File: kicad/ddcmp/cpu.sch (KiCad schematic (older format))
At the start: 9 parts, among them J1 UART, J4 LOOPTEST, U1 Pico

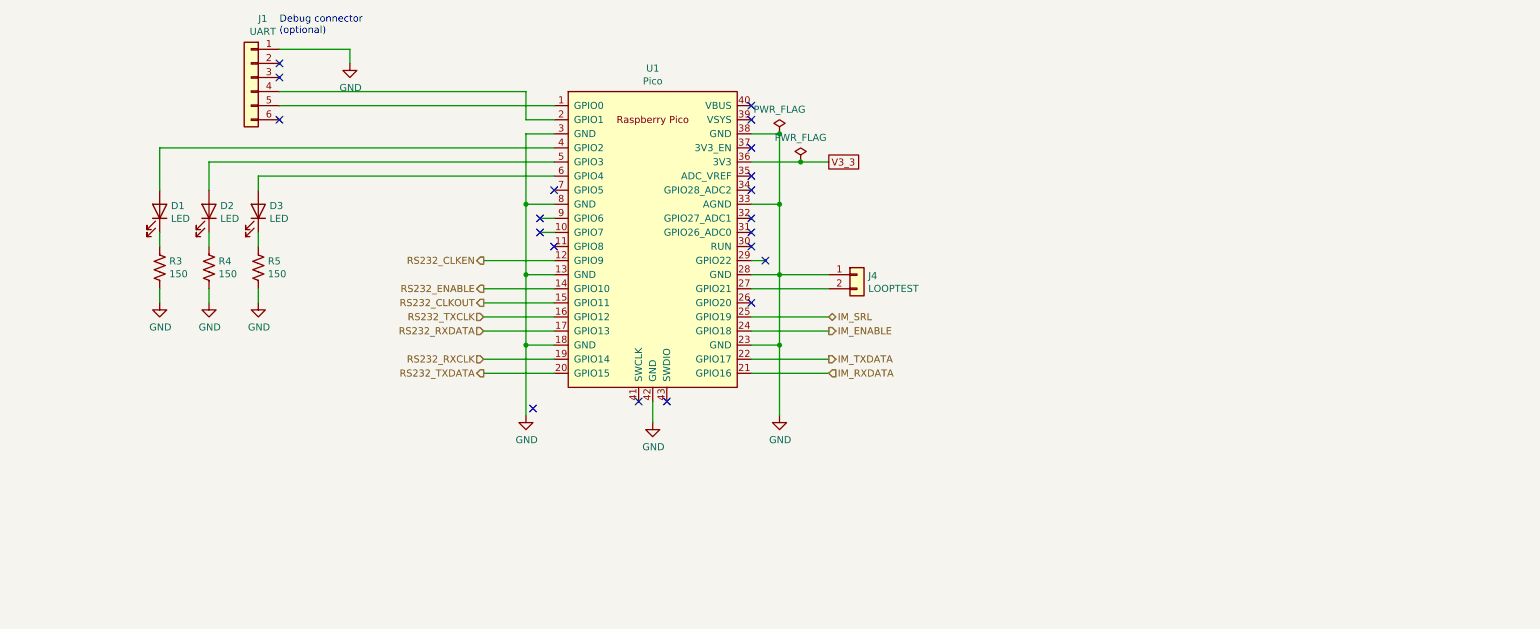
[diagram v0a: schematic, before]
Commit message: Finish the connector hookups, to be verified carefully against DMR-11 schematics.
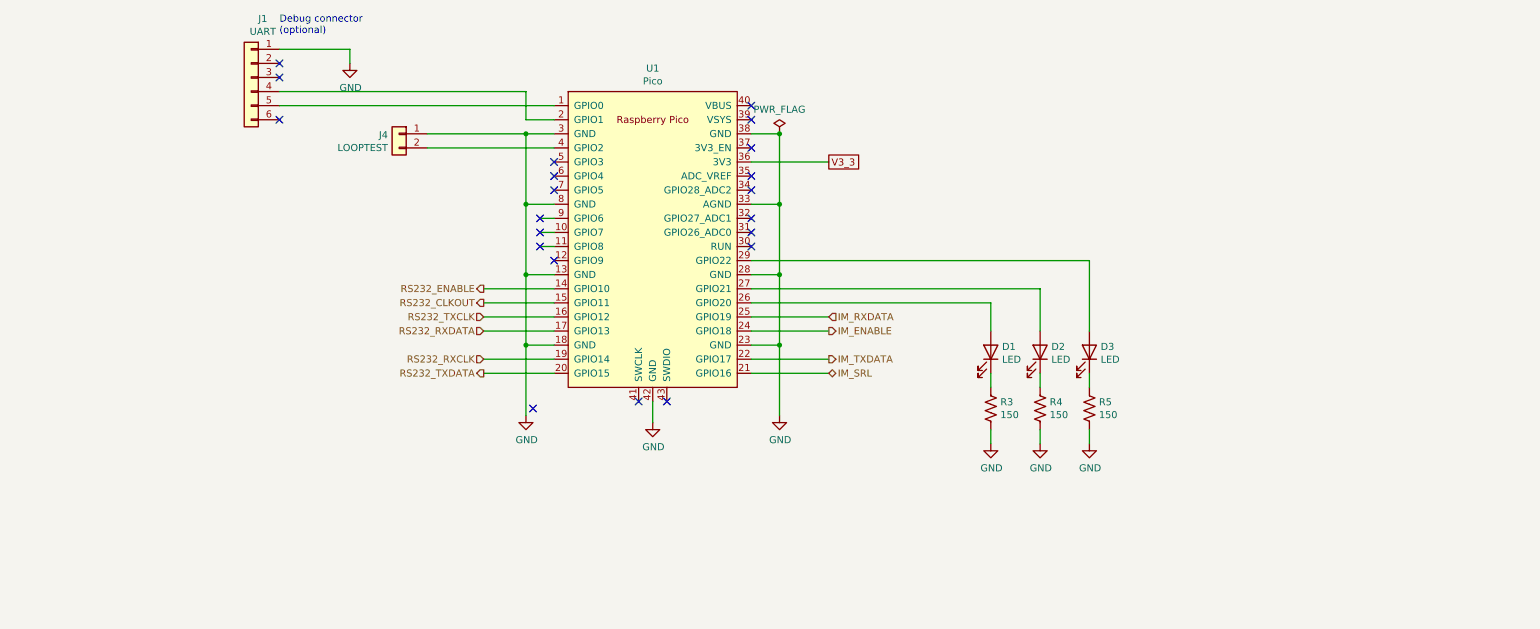
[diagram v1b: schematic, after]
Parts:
- U1: footprint RPi_Pico:RPi_Pico_SMD_TH -> ddcmp_parts:RPi_Pico_SMD_TH
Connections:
- net IM_RXDATA: now also U1.25 (GPIO19); no longer U1.21 (GPIO16)
- net IM_SRL: now also U1.21 (GPIO16); no longer U1.25 (GPIO19)
- net at U1.26 (GPIO20): now also D1.2 (A)
- net at U1.27 (GPIO21): now also D2.2 (A); no longer J4.2 (Pin_2)
- net at U1.29 (GPIO22): now also D3.2 (A)
- net at U1.4 (GPIO2): now also J4.2 (Pin_2); no longer D1.2 (A)
- net at U1.5 (GPIO3): no longer D2.2 (A)
- net at U1.6 (GPIO4): no longer D3.2 (A)
- net RS232_CLKEN: no longer names the net of U1.12 (GPIO9)
- no-connect marks 20 -> 21
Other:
- moved on the sheet: D1, D2, D3, J4, R3, R4, R5
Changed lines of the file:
@@
 Wire Wire Line
 	5050 4250 5050 4750
-Wire Wire Line
-	6650 2950 7000 2950
 Text GLabel 7200 2950 2    50   UnSpc ~ 0
 V3_3
@@
 L Device:LED D1
 U 1 1 60AC703D
-P 2450 3300
-F 0 "D1" V 2489 3380 50  0000 L CNN
-F 1 "LED" V 2398 3380 50  0000 L CNN
-F 2 "LEDs:LED_D3.0mm" H 2450 3300 50  0001 C CNN
-F 3 "~" H 2450 3300 50  0001 C CNN
-	1    2450 3300
+P 8350 4300
+F 0 "D1" V 8389 4380 50  0000 L CNN
+F 1 "LED" V 8298 4380 50  0000 L CNN
+F 2 "LEDs:LED_D3.0mm" H 8350 4300 50  0001 C CNN
+F 3 "~" H 8350 4300 50  0001 C CNN
+	1    8350 4300
 	0    1    -1   0
 $EndComp
@@
 L Device:LED D2
 U 1 1 60AC83AC
-P 2800 3300
-F 0 "D2" V 2839 3380 50  0000 L CNN
-F 1 "LED" V 2748 3380 50  0000 L CNN
-F 2 "LEDs:LED_D3.0mm" H 2800 3300 50  0001 C CNN
-F 3 "~" H 2800 3300 50  0001 C CNN
-	1    2800 3300
+P 8700 4300
+F 0 "D2" V 8739 4380 50  0000 L CNN
+F 1 "LED" V 8648 4380 50  0000 L CNN
+F 2 "LEDs:LED_D3.0mm" H 8700 4300 50  0001 C CNN
+F 3 "~" H 8700 4300 50  0001 C CNN
+	1    8700 4300
 	0    1    -1   0
 $EndComp
@@
 L Device:LED D3
 U 1 1 60AC89D4
-P 3150 3300
-F 0 "D3" V 3189 3380 50  0000 L CNN
-F 1 "LED" V 3098 3380 50  0000 L CNN
-F 2 "LEDs:LED_D3.0mm" H 3150 3300 50  0001 C CNN
-F 3 "~" H 3150 3300 50  0001 C CNN
-	1    3150 3300
+P 9050 4300
+F 0 "D3" V 9089 4380 50  0000 L CNN
+F 1 "LED" V 8998 4380 50  0000 L CNN
+F 2 "LEDs:LED_D3.0mm" H 9050 4300 50  0001 C CNN
+F 3 "~" H 9050 4300 50  0001 C CNN
+	1    9050 4300
 	0    1    -1   0
 $EndComp
@@
 L ddcmp_symbols:R_US R3
 U 1 1 60ACA428
-P 2450 3700
-F 0 "R3" H 2518 3746 50  0000 L CNN
-F 1 "150" H 2518 3655 50  0000 L CNN
-F 2 "ddcmp_parts:R_Axial_DIN0207_L6.3mm_D2.5mm_P7.62mm_Horizontal" V 2490 3690 50  0001 C CNN
-F 3 "" H 2450 3700 50  0001 C CNN
-	1    2450 3700
+P 8350 4700
+F 0 "R3" H 8418 4746 50  0000 L CNN
+F 1 "150" H 8418 4655 50  0000 L CNN
+F 2 "ddcmp_parts:R_Axial_DIN0207_L6.3mm_D2.5mm_P7.62mm_Horizontal" V 8390 4690 50  0001 C CNN
+F 3 "" H 8350 4700 50  0001 C CNN
+	1    8350 4700
 	1    0    0    -1
 $EndComp
@@
 L ddcmp_symbols:R_US R4
 U 1 1 60ACAA45
-P 2800 3700
-F 0 "R4" H 2868 3746 50  0000 L CNN
-F 1 "150" H 2868 3655 50  0000 L CNN
-F 2 "ddcmp_parts:R_Axial_DIN0207_L6.3mm_D2.5mm_P7.62mm_Horizontal" V 2840 3690 50  0001 C CNN
-F 3 "" H 2800 3700 50  0001 C CNN
-	1    2800 3700
+P 8700 4700
+F 0 "R4" H 8768 4746 50  0000 L CNN
+F 1 "150" H 8768 4655 50  0000 L CNN
+F 2 "ddcmp_parts:R_Axial_DIN0207_L6.3mm_D2.5mm_P7.62mm_Horizontal" V 8740 4690 50  0001 C CNN
+F 3 "" H 8700 4700 50  0001 C CNN
+	1    8700 4700
 	1    0    0    -1
 $EndComp
@@
 L ddcmp_symbols:R_US R5
 U 1 1 60ACB075
-P 3150 3700
-F 0 "R5" H 3218 3746 50  0000 L CNN
-F 1 "150" H 3218 3655 50  0000 L CNN
-F 2 "ddcmp_parts:R_Axial_DIN0207_L6.3mm_D2.5mm_P7.62mm_Horizontal" V 3190 3690 50  0001 C CNN
-F 3 "" H 3150 3700 50  0001 C CNN
-	1    3150 3700
+P 9050 4700
+F 0 "R5" H 9118 4746 50  0000 L CNN
+F 1 "150" H 9118 4655 50  0000 L CNN
+F 2 "ddcmp_parts:R_Axial_DIN0207_L6.3mm_D2.5mm_P7.62mm_Horizontal" V 9090 4690 50  0001 C CNN
+F 3 "" H 9050 4700 50  0001 C CNN
+	1    9050 4700
 	1    0    0    -1
 $EndComp
@@
 L power:GND #PWR0111
 U 1 1 60ACBBD7
-P 2450 3950
-F 0 "#PWR0111" H 2450 3700 50  0001 C CNN
-F 1 "GND" H 2455 3777 50  0000 C CNN
-F 2 "" H 2450 3950 50  0001 C CNN
-F 3 "" H 2450 3950 50  0001 C CNN
-	1    2450 3950
+P 8350 4950
+F 0 "#PWR0111" H 8350 4700 50  0001 C CNN
+F 1 "GND" H 8355 4777 50  0000 C CNN
+F 2 "" H 8350 4950 50  0001 C CNN
+F 3 "" H 8350 4950 50  0001 C CNN
+	1    8350 4950
 	1    0    0    -1
 $EndComp
@@
 L power:GND #PWR0112
 U 1 1 60ACC03F
-P 2800 3950
-F 0 "#PWR0112" H 2800 3700 50  0001 C CNN
-F 1 "GND" H 2805 3777 50  0000 C CNN
-F 2 "" H 2800 3950 50  0001 C CNN
-F 3 "" H 2800 3950 50  0001 C CNN
-	1    2800 3950
+P 8700 4950
+F 0 "#PWR0112" H 8700 4700 50  0001 C CNN
+F 1 "GND" H 8705 4777 50  0000 C CNN
+F 2 "" H 8700 4950 50  0001 C CNN
+F 3 "" H 8700 4950 50  0001 C CNN
+	1    8700 4950
 	1    0    0    -1
 $EndComp
@@
 L power:GND #PWR0113
 U 1 1 60ACC9AB
-P 3150 3950
-F 0 "#PWR0113" H 3150 3700 50  0001 C CNN
-F 1 "GND" H 3155 3777 50  0000 C CNN
-F 2 "" H 3150 3950 50  0001 C CNN
-F 3 "" H 3150 3950 50  0001 C CNN
-	1    3150 3950
-	1    0    0    -1
-$EndComp
-Wire Wire Line
-	3150 3950 3150 3850
-Wire Wire Line
-	2800 3950 2800 3850
-Wire Wire Line
-	2450 3950 2450 3850
-Wire Wire Line
-	2450 3550 2450 3450
-Wire Wire Line
-	2800 3550 2800 3450
-Wire Wire Line
-	3150 3550 3150 3450
-Wire Wire Line
-	2450 3150 2450 2850
-Wire Wire Line
-	2800 2950 2800 3150
-Wire Wire Line
-	3150 3150 3150 3050
-Wire Wire Line
-	2450 2850 5250 2850
-Wire Wire Line
-	2800 2950 5250 2950
-Wire Wire Line
-	3150 3050 5250 3050
-Wire Wire Line
-	6650 4450 7200 4450
+P 9050 4950
+F 0 "#PWR0113" H 9050 4700 50  0001 C CNN
+F 1 "GND" H 9055 4777 50  0000 C CNN
+F 2 "" H 9050 4950 50  0001 C CNN
+F 3 "" H 9050 4950 50  0001 C CNN
+	1    9050 4950
+	1    0    0    -1
+$EndComp
+Wire Wire Line
+	9050 4950 9050 4850
+Wire Wire Line
+	8700 4950 8700 4850
+Wire Wire Line
+	8350 4950 8350 4850
+Wire Wire Line
+	8350 4550 8350 4450
+Wire Wire Line
+	8700 4550 8700 4450
+Wire Wire Line
+	9050 4550 9050 4450
 Wire Wire Line
 	6650 4350 7200 4350
@@
 	6650 4150 7200 4150
 Wire Wire Line
-	5250 3650 4750 3650
-Wire Wire Line
 	5250 3850 4750 3850
 Wire Wire Line
@@
 Wire Wire Line
 	5250 4450 4750 4450
-Wire Wire Line
-	6650 4050 7200 4050
-Text HLabel 7200 4050 2    50   3State ~ 0
+Text HLabel 7200 4450 2    50   3State ~ 0
 IM_SRL
 Text HLabel 7200 4150 2    50   Output ~ 0
@@
 Text HLabel 7200 4350 2    50   Output ~ 0
 IM_TXDATA
-Text HLabel 7200 4450 2    50   Input ~ 0
+Text HLabel 7200 4050 2    50   Input ~ 0
 IM_RXDATA
-Text HLabel 4750 3650 0    50   Output ~ 0
-RS232_CLKEN
 Text HLabel 4750 3850 0    50   Output ~ 0
 RS232_ENABLE
@@
 Wire Wire Line
 	5250 3450 5150 3450
-Wire Wire Line
-	6650 3650 6750 3650
-NoConn ~ 6750 3650
 NoConn ~ 5150 3350
 NoConn ~ 5150 3450
@@
 L Connector_Generic:Conn_01x02 J4
 U 1 1 60AFBDD5
-P 7400 3750
-F 0 "J4" H 7480 3742 50  0000 L CNN
-F 1 "LOOPTEST" H 7480 3651 50  0000 L CNN
-F 2 "Pin_Headers:Pin_Header_Straight_1x02_Pitch2.54mm" H 7400 3750 50  0001 C CNN
-F 3 "~" H 7400 3750 50  0001 C CNN
-	1    7400 3750
-	1    0    0    -1
-$EndComp
-Wire Wire Line
-	7200 3750 6850 3750
-Wire Wire Line
-	7200 3850 6650 3850
+P 4150 2750
+F 0 "J4" H 4230 2742 50  0000 L CNN
+F 1 "LOOPTEST" H 4230 2651 50  0000 L CNN
+F 2 "Pin_Headers:Pin_Header_Straight_1x02_Pitch2.54mm" H 4150 2750 50  0001 C CNN
+F 3 "~" H 4150 2750 50  0001 C CNN
+	1    4150 2750
+	-1   0    0    -1
+$EndComp
 NoConn ~ 3300 2250
 NoConn ~ 3300 2350
 NoConn ~ 3300 2650
 NoConn ~ 5250 3150
-NoConn ~ 5250 3550
 NoConn ~ 6650 2550
 NoConn ~ 6650 2650
@@
 NoConn ~ 6650 3450
 NoConn ~ 6650 3550
-NoConn ~ 6650 3950
 NoConn ~ 5100 4700
 NoConn ~ 5850 4650
@@
 Connection ~ 6850 2750
 $Comp
-L power:PWR_FLAG #FLG0102
-U 1 1 60B1F957
-P 7000 2950
-F 0 "#FLG0102" H 7000 3025 50  0001 C CNN
-F 1 "PWR_FLAG" H 7000 3123 50  0000 C CNN
-F 2 "" H 7000 2950 50  0001 C CNN
-F 3 "~" H 7000 2950 50  0001 C CNN
-	1    7000 2950
-	1    0    0    -1
-$EndComp
-Connection ~ 7000 2950
-Wire Wire Line
-	7000 2950 7200 2950
-$Comp
 L ddcmp_symbols:Raspberry_Pico U?
 U 1 1 60A47CFF
@@
 F 0 "U1" H 5950 4715 50  0000 C CNN
 F 1 "Pico" H 5950 4624 50  0000 C CNN
-F 2 "RPi_Pico:RPi_Pico_SMD_TH" V 5950 3500 50  0001 C CNN
+F 2 "ddcmp_parts:RPi_Pico_SMD_TH" V 5950 3500 50  0001 C CNN
 F 3 "" H 5950 3500 50  0001 C CNN
 	1    5950 3500
 	1    0    0    -1
 $EndComp
+Wire Wire Line
+	6650 2950 7200 2950
+Wire Wire Line
+	6650 4450 7200 4450
+Wire Wire Line
+	7200 4050 6650 4050
+Wire Wire Line
+	5050 2750 4350 2750
+Connection ~ 5050 2750
+Wire Wire Line
+	4350 2850 5250 2850
+Wire Wire Line
+	6650 3950 8350 3950
+Wire Wire Line
+	8350 3950 8350 4150
+Wire Wire Line
+	8700 4150 8700 3850
+Wire Wire Line
+	8700 3850 6650 3850
+Wire Wire Line
+	6650 3650 9050 3650
+Wire Wire Line
+	9050 3650 9050 4150
+Wire Wire Line
+	5250 3550 5150 3550
+NoConn ~ 5150 3550
+NoConn ~ 5250 3650
+NoConn ~ 5250 3050
+NoConn ~ 5250 2950
 $EndSCHEMATC
